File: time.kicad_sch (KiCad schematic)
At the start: 12 parts, among them J15 Conn_01x03_Socket, J5 Conn_01x02_Socket, U6 AM1815, Y1 32.768k

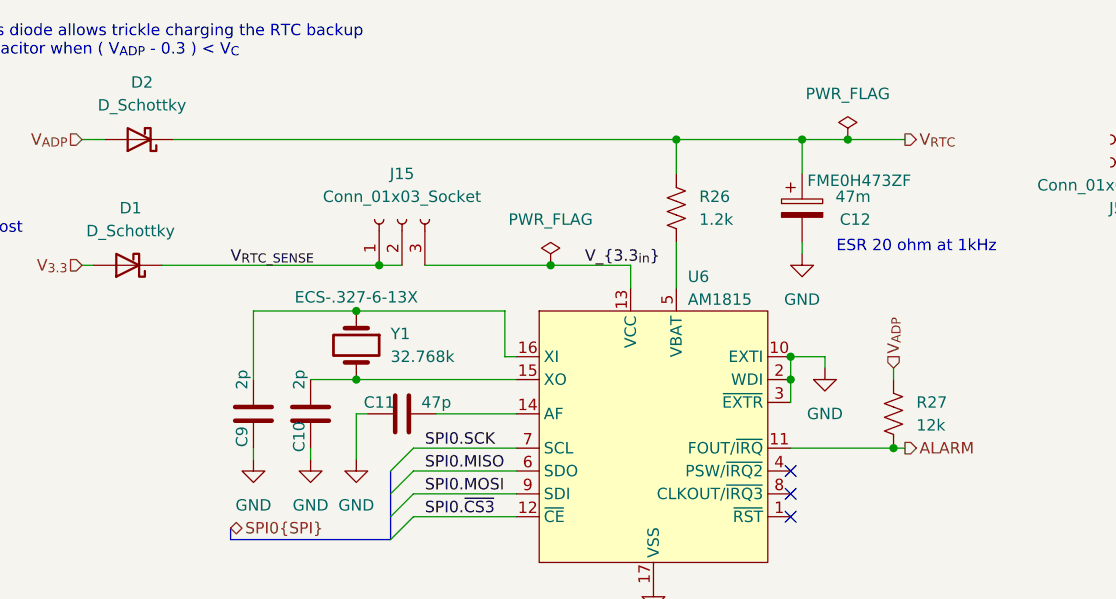
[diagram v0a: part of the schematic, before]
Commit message: Add more informative text, crystal to SMD, headers
 - Added a lot more to the silkscreen to segment parts of the board
 - Changed the 32kHz crystals to an SMD part
 - Added some headers for ADP5091 function
 - Some BOM consolidation, mostly of resistors and capacitors
 - Marked one capacitor as C0G rating
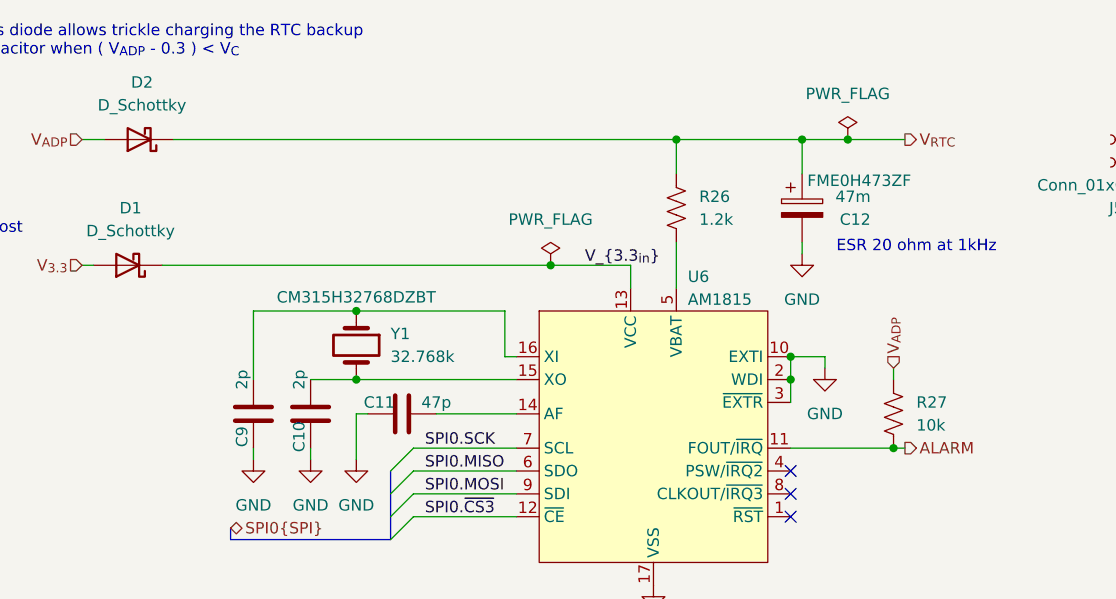
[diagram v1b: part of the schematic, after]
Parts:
- removed J15: Conn_01x03_Socket, Connector_PinHeader_2.54mm:PinHeader_1x03_P2.54mm_Vertical, symbol Connector:Conn_01x03_Socket
- C12: Digikey Product Number (none) -> 399-13100-ND
- R27: value 12k -> 10k
- Y1: footprint Crystal:Crystal_DS26_D2.0mm_L6.0mm_Vertical -> Marcano:CM315H; Digikey Product Number XC2293-ND -> 300-CM315H32768DZBTTR-ND; Manufacturer Product Number ECS-.327-6-13X -> CM315H32768DZBT
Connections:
- net V_{RTC_SENSE} is gone; now on net V_{3.3_{in}}: D1.1 (K)
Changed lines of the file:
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@@
-		(color 0 0 0 0)
-	)
-	(junction
-		(at 105.41 76.2)
-		(diameter 0)
 		(color 0 0 0 0)
 	)
@@
 		)
 	)
-	(wire
-		(pts
-			(xy 81.28 76.2) (xy 105.41 76.2)
-		)
-		(stroke
-			(width 0)
-			(type default)
-		)
-	)
 	(bus
 		(pts
@@
 		)
 	)
-	(wire
-		(pts
-			(xy 110.49 76.2) (xy 124.46 76.2)
-		)
-		(stroke
-			(width 0)
-			(type default)
-		)
-	)
 	(bus
 		(pts
@@
 	(wire
 		(pts
-			(xy 105.41 76.2) (xy 107.95 76.2)
+			(xy 81.28 76.2) (xy 124.46 76.2)
 		)
 		(stroke
@@
 	(label "SPI0.~{CS3}"
 		(at 110.49 104.14 0)
-		(fields_autoplaced yes)
-		(effects
-			(font
-				(size 1.27 1.27)
-			)
-			(justify left bottom)
-		)
-	)
-	(label "V_{RTC_SENSE}"
-		(at 88.9 76.2 0)
 		(fields_autoplaced yes)
 		(effects
@@
 			)
 		)
-		(property "Footprint" "Crystal:Crystal_DS26_D2.0mm_L6.0mm_Vertical"
+		(property "Footprint" "Marcano:CM315H"
 			(at 102.87 85.09 0)
 			(effects
@@
 			)
 		)
-		(property "Datasheet" "~"
+		(property "Datasheet" "https://cfd.citizen.co.jp/cms/cfd/pdf/english/CM315H_E.pdf"
 			(at 102.87 85.09 0)
 			(effects
@@
 			)
 		)
-		(property "Manufacturer Product Number" "ECS-.327-6-13X"
+		(property "Manufacturer Product Number" "CM315H32768DZBT"
 			(at 102.87 79.756 90)
 			(effects
@@
 			)
 		)
-		(property "Digikey Product Number" "XC2293-ND"
+		(property "Digikey Product Number" "300-CM315H32768DZBTTR-ND"
 			(at 102.87 85.09 0)
 			(effects
@@
 			)
 		)
-		(property "Datasheet" "~"
+		(property "Datasheet" "https://connect.kemet.com:7667/gateway/IntelliData-ComponentDocumentation/1.0/download/datasheet/FME0H473ZF"
 			(at 152.4 69.85 0)
 			(effects
@@
 			)
 		)
-		(property "Digikey Product Number" ""
+		(property "Digikey Product Number" "399-13100-ND"
 			(at 152.4 69.85 0)
 			(effects
@@
 	)
 	(symbol
-		(lib_id "Connector:Conn_01x03_Socket")
-		(at 107.95 71.12 90)
-		(unit 1)
-		(exclude_from_sim no)
-		(in_bom yes)
-		(on_board yes)
-		(dnp no)
-		(fields_autoplaced yes)
-		(property "Reference" "J15"
-			(at 107.95 66.04 90)
-			(effects
-				(font
-					(size 1.27 1.27)
-				)
-			)
-		)
-		(property "Value" "Conn_01x03_Socket"
-			(at 107.95 68.58 90)
-			(effects
-				(font
-					(size 1.27 1.27)
-				)
-			)
-		)
-		(property "Footprint" "Connector_PinHeader_2.54mm:PinHeader_1x03_P2.54mm_Vertical"
-			(at 107.95 71.12 0)
-			(effects
-				(font
-					(size 1.27 1.27)
-				)
-				(hide yes)
-			)
-		)
-		(property "Datasheet" "~"
-			(at 107.95 71.12 0)
-			(effects
-				(font
-					(size 1.27 1.27)
-				)
-				(hide yes)
-			)
-		)
-		(property "Description" "Generic connector, single row, 01x03, script generated"
-			(at 107.95 71.12 0)
-			(effects
-				(font
-					(size 1.27 1.27)
-				)
-				(hide yes)
-			)
-		)
-		(pin "2"
-		)
-		(pin "3"
-		)
-		(pin "1"
-		)
-		(instances
-			(project "artemia"
-				(path "/3ef271cf-72c1-43e9-bc06-d7d78e288e38/9bab1f2e-658f-484a-8e5a-6de6f47dc750"
-					(reference "J15")
-					(unit 1)
-				)
-			)
-		)
-	)
-	(symbol
 		(lib_id "power:PWR_FLAG")
 		(at 124.46 76.2 0)
@@
 			)
 		)
-		(property "Value" "12k"
+		(property "Value" "10k"
 			(at 165.1 93.98 0)
 			(effects

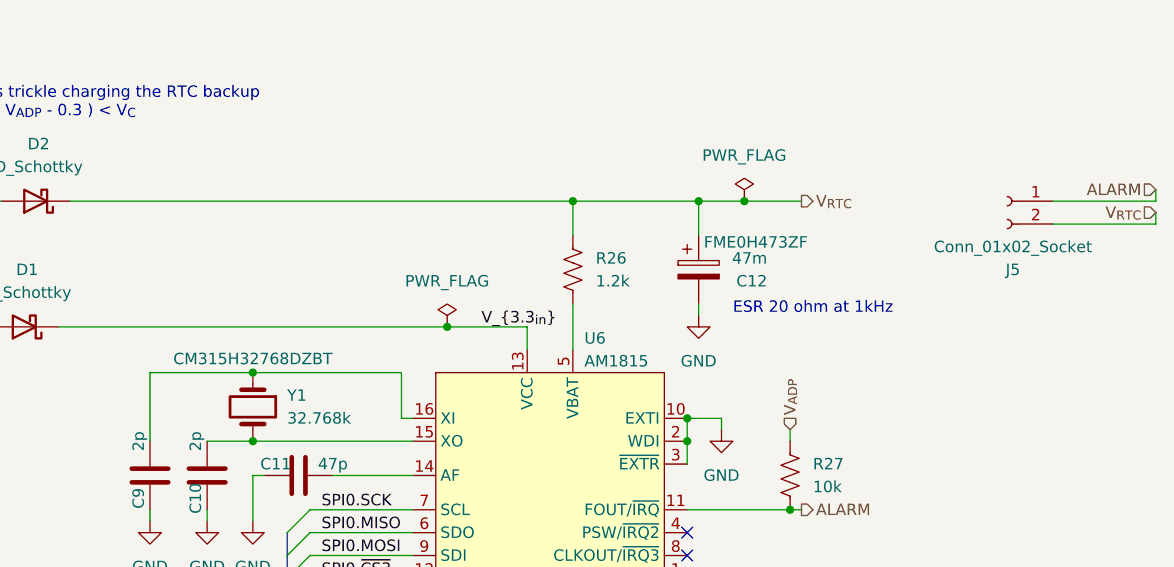
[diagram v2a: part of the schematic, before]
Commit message: Update datasheet and MPN for C and R
 - Update pin headers from sockets to pins
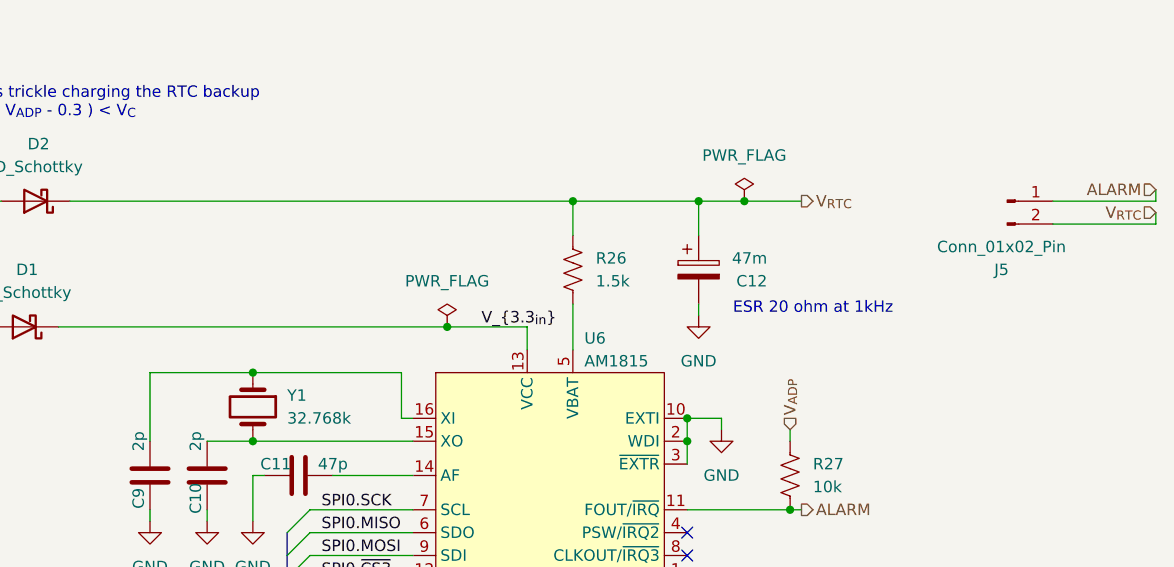
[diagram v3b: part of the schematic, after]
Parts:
- C10, C9: Digikey Product Number (none) -> 1276-2124-2-ND; Manufacturer Product Number (none) -> CL10C020CB8NNNC
- C11: Digikey Product Number (none) -> 1276-1037-2-ND; Manufacturer Product Number (none) -> CL10C470JB8NNNC
- J5: value Conn_01x02_Socket -> Conn_01x02_Pin; symbol Connector:Conn_01x02_Socket -> Connector:Conn_01x02_Pin
- R26: value 1.2k -> 1.5k; Digikey Product Number (none) -> 1292-WR06X1501FTLTR-ND; Manufacturer Product Number (none) -> WR06X1501FTL
- R27: Digikey Product Number (none) -> RMCF0603FT10K0TR-ND; Manufacturer Product Number (none) -> RMCF0603FT10K0
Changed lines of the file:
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@@
 					(size 1.27 1.27)
 				)
+				(hide yes)
 			)
 		)
@@
 			)
 		)
+		(property "Digikey Product Number" "1276-2124-2-ND"
+			(at 91.44 92.71 0)
+			(effects
+				(font
+					(size 1.27 1.27)
+				)
+				(hide yes)
+			)
+		)
+		(property "Manufacturer Product Number" "CL10C020CB8NNNC"
+			(at 91.44 92.71 0)
+			(effects
+				(font
+					(size 1.27 1.27)
+				)
+				(hide yes)
+			)
+		)
 		(pin "1"
 		)
@@
 			)
 		)
-		(property "Datasheet" "~"
+		(property "Datasheet" "https://mm.digikey.com/Volume0/opasdata/d220001/medias/docus/609/CL10C470JB8NNNC_Spec.pdf"
 			(at 107.95 92.71 0)
 			(effects
@@
 		)
 		(property "Description" "Unpolarized capacitor"
+			(at 107.95 92.71 0)
+			(effects
+				(font
+					(size 1.27 1.27)
+				)
+				(hide yes)
+			)
+		)
+		(property "Digikey Product Number" "1276-1037-2-ND"
+			(at 107.95 92.71 0)
+			(effects
+				(font
+					(size 1.27 1.27)
+				)
+				(hide yes)
+			)
+		)
+		(property "Manufacturer Product Number" "CL10C470JB8NNNC"
 			(at 107.95 92.71 0)
 			(effects
@@
 					(size 1.27 1.27)
 				)
+				(hide yes)
 			)
 		)
@@
 	)
 	(symbol
-		(lib_id "Connector:Conn_01x02_Socket")
+		(lib_id "Connector:Conn_01x02_Pin")
 		(at 186.69 62.23 0)
-		(mirror y)
 		(unit 1)
 		(exclude_from_sim no)
@@
 		(dnp no)
 		(property "Reference" "J5"
-			(at 187.325 69.85 0)
-			(effects
-				(font
-					(size 1.27 1.27)
-				)
-			)
-		)
-		(property "Value" "Conn_01x02_Socket"
-			(at 187.325 67.31 0)
+			(at 186.055 69.85 0)
+			(effects
+				(font
+					(size 1.27 1.27)
+				)
+			)
+		)
+		(property "Value" "Conn_01x02_Pin"
+			(at 186.055 67.31 0)
 			(effects
 				(font
@@
 			)
 		)
-		(property "Value" "1.2k"
+		(property "Value" "1.5k"
 			(at 140.97 71.12 0)
 			(effects
@@
 			)
 		)
-		(property "Datasheet" "~"
+		(property "Datasheet" "http://www.passivecomponent.com/wp-content/uploads/chipR/ASC_WR.pdf"
 			(at 138.43 69.85 0)
 			(effects
@@
 		)
 		(property "Description" "Resistor, US symbol"
+			(at 138.43 69.85 0)
+			(effects
+				(font
+					(size 1.27 1.27)
+				)
+				(hide yes)
+			)
+		)
+		(property "Digikey Product Number" "1292-WR06X1501FTLTR-ND"
+			(at 138.43 69.85 0)
+			(effects
+				(font
+					(size 1.27 1.27)
+				)
+				(hide yes)
+			)
+		)
+		(property "Manufacturer Product Number" "WR06X1501FTL"
 			(at 138.43 69.85 0)
 			(effects
@@
 			)
 		)
+		(property "Digikey Product Number" "1276-2124-2-ND"
+			(at 97.79 92.71 0)
+			(effects
+				(font
+					(size 1.27 1.27)
+				)
+				(hide yes)
+			)
+		)
+		(property "Manufacturer Product Number" "CL10C020CB8NNNC"
+			(at 97.79 92.71 0)
+			(effects
+				(font
+					(size 1.27 1.27)
+				)
+				(hide yes)
+			)
+		)
 		(pin "1"
 		)
@@
 			)
 		)
-		(property "Datasheet" "~"
+		(property "Datasheet" "https://www.seielect.com/catalog/sei-rmcf_rmcp.pdf"
 			(at 162.56 92.71 0)
 			(effects
@@
 			(at 162.56 92.71 0)
 			(effects
+				(font
+					(size 1.27 1.27)
+				)
+				(hide yes)
+			)
+		)
+		(property "Digikey Product Number" "RMCF0603FT10K0TR-ND"
+			(at 162.56 92.71 0)
+			(effects
+				(font
+					(size 1.27 1.27)
+				)
+				(hide yes)
+			)
+		)
+		(property "Manufacturer Product Number" "RMCF0603FT10K0"
+			(at 162.56 92.71 0)
+			(effects

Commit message: Fix BSS123 pins, remove R18 R19 pulldowns
 - BSS123 pinout were completely wrong due to using the wrong symbol in
   the schematic. Made a new symbol with the right pinout. Fixes #7.
 - R18 and R19 were forming a voltage divider as V_GOOD and EN_PULSE
   are open-drain lines. Remove the pull-downs, and pray that circuit
   initialization is sane. Fixes #6.
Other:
- title: Artemia: Time Subsystem -> Artemia: Power Management Subsystem
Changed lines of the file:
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@@
 	(paper "USLetter")
 	(title_block
-		(title "Artemia: Time Subsystem")
-		(date "2024-04-09")
-		(rev "A")
+		(title "Artemia: Power Management Subsystem")
+		(date "2024-11-21")
+		(rev "B*")
 		(company "UC San Diego")
 		(comment 1 "Author: ${AUTHOR}")
